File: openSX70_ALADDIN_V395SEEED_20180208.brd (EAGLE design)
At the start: 95.9 x 27.9 mm, 44 parts, among them J1 GND, Q1 2N7002, Q2 2N7002, U1 ATMEGA328P_TQFP, U3 BH1750FVI-TR, Y1 CSTCE8M00G52Z-R0

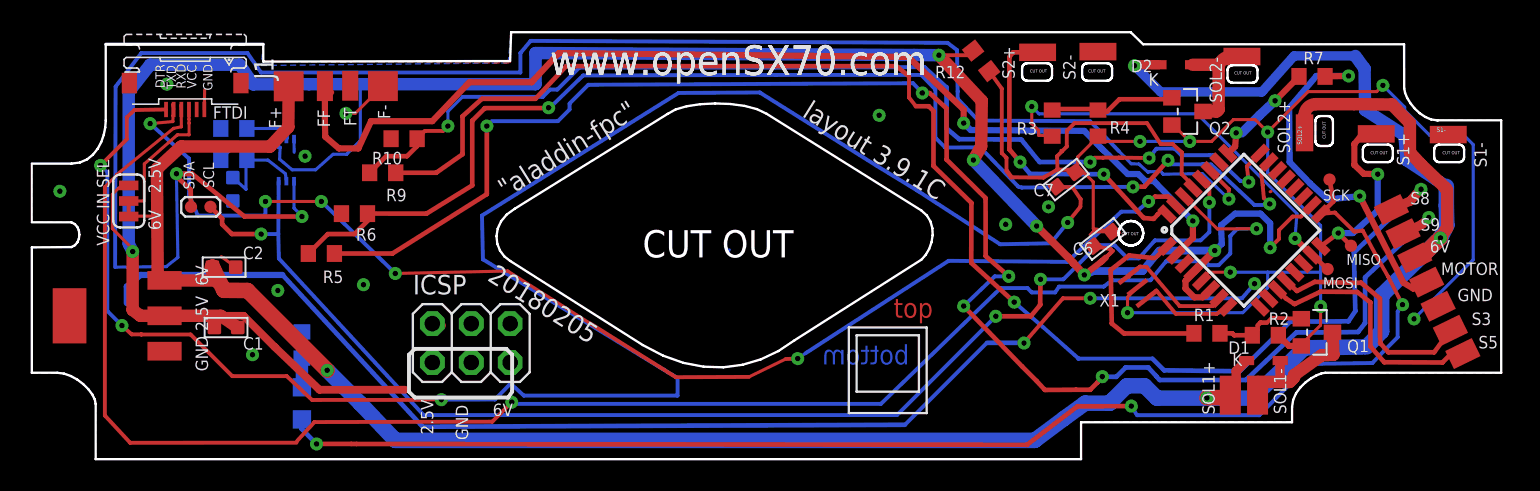
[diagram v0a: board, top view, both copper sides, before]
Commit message: NEW VERSION 3.9.5S for SeeedStudio Fusion PCBA test
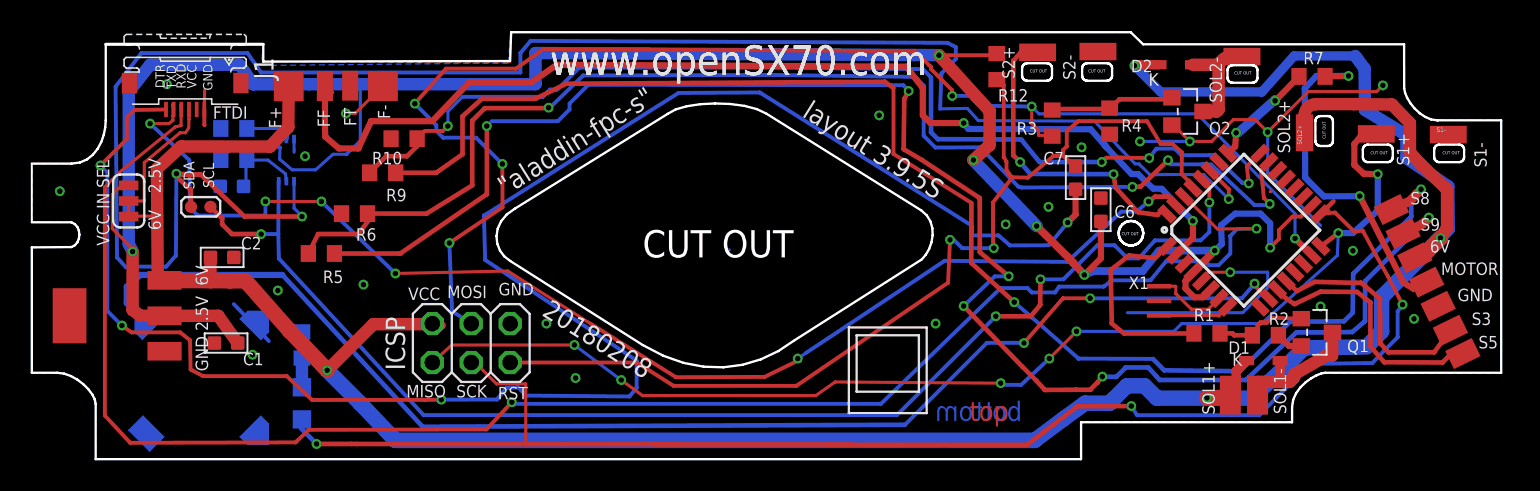
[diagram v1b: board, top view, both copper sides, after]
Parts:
- removed MISO, MOSI, SCK: PTR1TP08R, testpad:TP08R
- added U$3: CSET8-5G_V2, openSX70:CSET8-5G_PACKAGE
- moved C6 1.91 mm to (71.8, 17.1), turned to 180 degrees
- moved Y1 1.59 mm to (75.4, 11.2), turned to 270 degrees
- moved R12 1.09 mm to (65.0, 26.4), turned to 90 degrees
- moved C1 1.02 mm to (14.7, 8.38)
- moved R4 0.77 mm to (72.4, 22.9)
- moved C7 0.65 mm to (70.2, 19.2), turned to 180 degrees
- moved C2 0.65 mm to (14.5, 14.0)
- moved C5 0.20 mm to (15.1, 18.6), turned to 90 degrees
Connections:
- net BUZZER: now also U$3.+
- net GND: now also U$3.GND
- net LED: no longer SCK.TP
- net S1: no longer MISO.TP
- net SOL2: no longer MOSI.TP
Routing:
- net S1: track 13.0 -> 77.8 mm, vias 2 -> 7
- net SOL2: track 27.7 -> 90.2 mm, vias 2 -> 6
- net GND: track 98.0 -> 54.6 mm, vias 18 -> 22
- net RST: track 26.0 -> 68.0 mm, vias 0 -> 2
- net 3.3V: track 168.4 -> 152.8 mm
- net 6V: track 180.8 -> 190.2 mm
- net LED: track 89.4 -> 96.0 mm
- net DTR: track 123.4 -> 118.4 mm
- net N$4: track 7.74 -> 5.15 mm
- net SDA: track 121.4 -> 123.9 mm
- net S8@6V: track 94.0 -> 91.8 mm
- net BUZZER: track 85.1 -> 87.2 mm
- net N$6: track 6.62 -> 4.79 mm
- net N$2: track 6.43 -> 5.53 mm
- net MOTOR-HEADER: track 23.6 -> 22.7 mm
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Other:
- board text added: ""aladdin-fpc-S""
- board text added: ""aladdin-fpc-s""
- board text added: "20180208"
- board text added: "MISO"
- board text added: "MOSI"
- board text added: "RST"
- board text added: "SCK"
- board text added: "layout 3.9.5S"
- board text added: "openSX70 project visit www.openSX70.com version 3.9.5S "Aladdin-fpc-S" 20170208 by Joaquín de Prada"
- board text removed: ""aladdin-fpc""
- board text removed: "20180205"
- board text removed: "DUMMY"
- board text removed: "layout 3.9.1C"
- board text removed: "openSX70 project visit www.openSX70.com version 3.9.1 "aladdin-fpc" 20170125 by Joaquín de Prada"

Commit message: Removed unnecessary vias, al pads. Minor fixes all over. Getting ready for production!
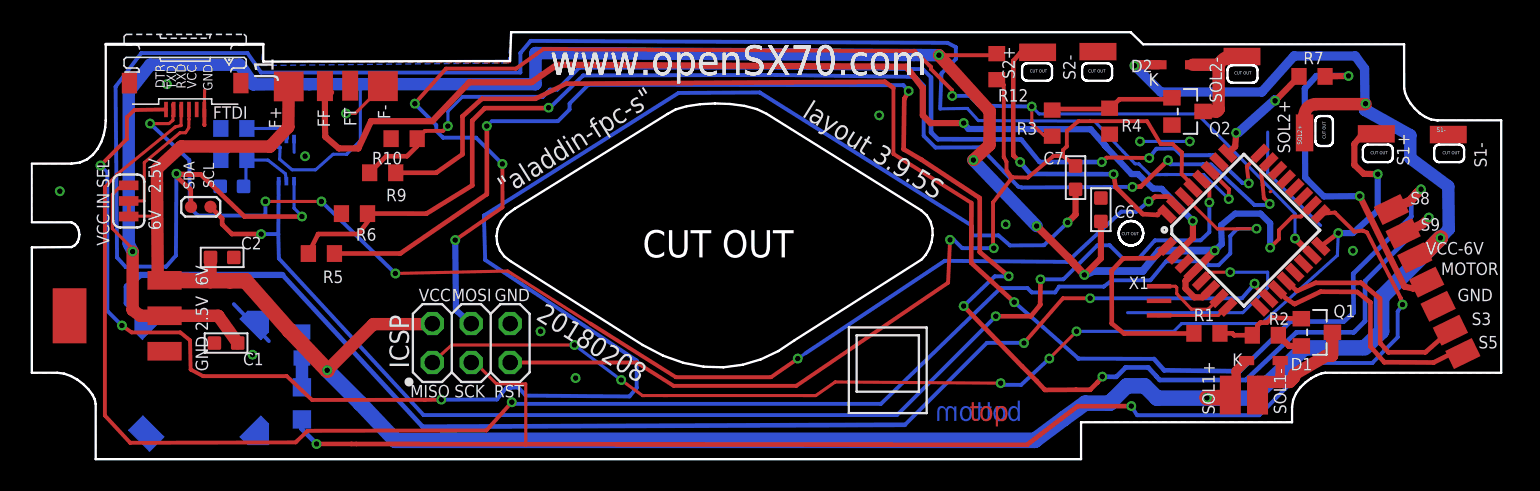
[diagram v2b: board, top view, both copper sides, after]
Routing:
- net GND: track 54.6 -> 38.4 mm, vias 22 -> 13
- net 6V: track 190.2 -> 178.9 mm, vias 4 -> 5
- net LED: track 96.0 -> 95.0 mm
- net SOL2: track 90.2 -> 89.6 mm
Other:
- board text added: "VCC-6V"
